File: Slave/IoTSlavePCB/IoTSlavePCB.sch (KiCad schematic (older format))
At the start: 0 parts

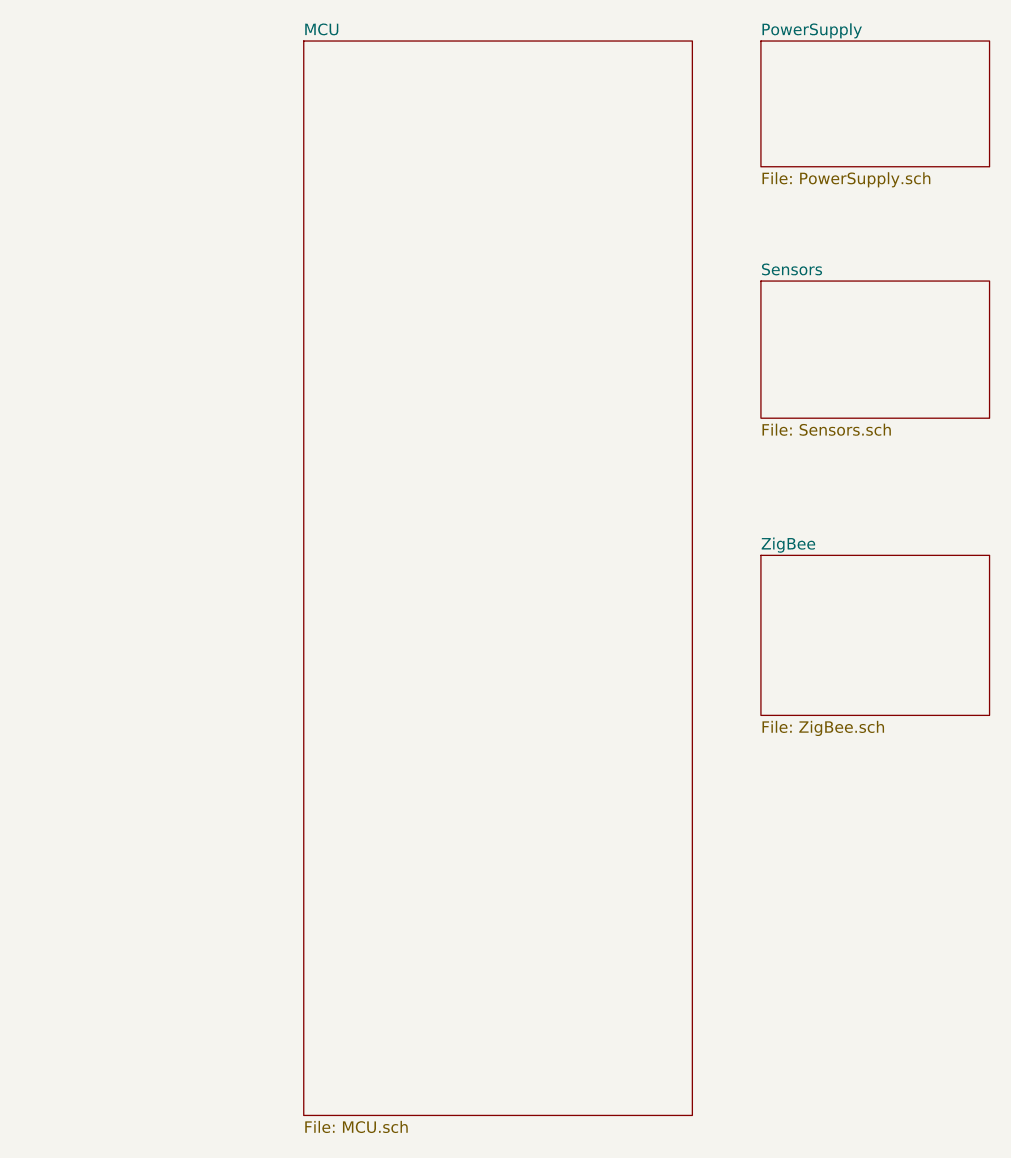
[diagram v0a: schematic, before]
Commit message: Continued work on slaves. Added sensor and begun work on ZigBee transceiver.
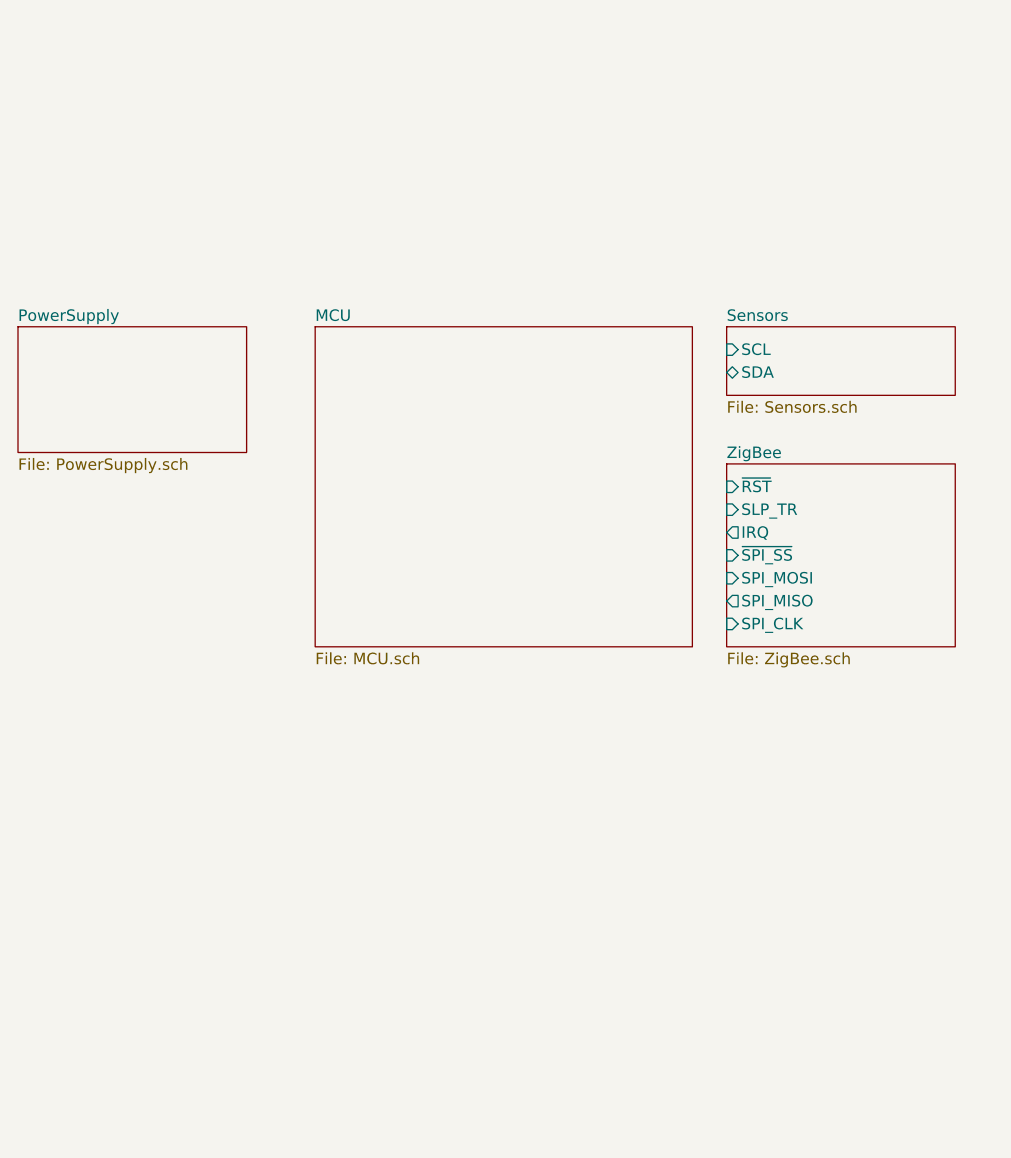
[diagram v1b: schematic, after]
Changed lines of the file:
@@
 $EndDescr
 $Sheet
-S 4700 1400 1700 4700
+S 4750 2650 1650 1400
 U 5F9E756E
 F0 "MCU" 50
@@
 $EndSheet
 $Sheet
-S 6700 1400 1000 550
+S 3450 2650 1000 550
 U 5F9F06B0
 F0 "PowerSupply" 50
@@
 $EndSheet
 $Sheet
-S 6700 2450 1000 600
+S 6550 2650 1000 300
 U 5F9F077B
 F0 "Sensors" 50
 F1 "Sensors.sch" 50
+F2 "SCL" I L 6550 2750 50
+F3 "SDA" B L 6550 2850 50
 $EndSheet
 $Sheet
-S 6700 3650 1000 700
+S 6550 3250 1000 800
 U 5F9F085D
 F0 "ZigBee" 50
 F1 "ZigBee.sch" 50
+F2 "~RST" I L 6550 3350 50
+F3 "SLP_TR" I L 6550 3450 50
+F4 "IRQ" O L 6550 3550 50
+F5 "~SPI_SS" I L 6550 3650 50
+F6 "SPI_MOSI" I L 6550 3750 50
+F7 "SPI_MISO" O L 6550 3850 50
+F8 "SPI_CLK" I L 6550 3950 50
 $EndSheet
 $EndSCHEMATC

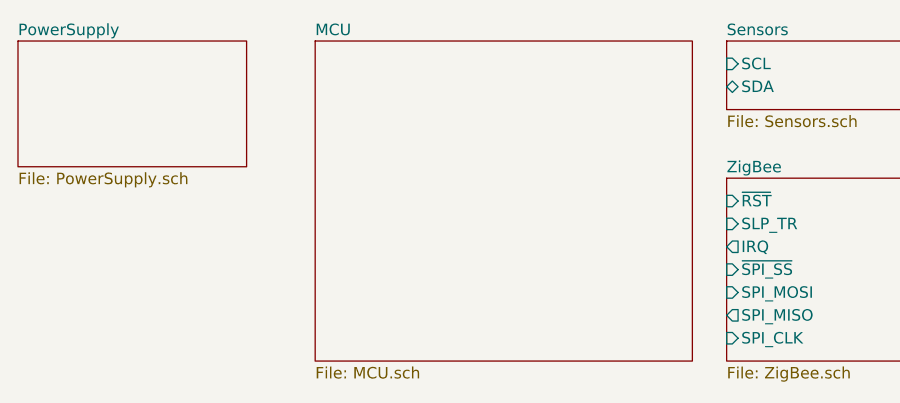
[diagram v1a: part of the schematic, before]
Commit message: Finished slave schematics, including memory and Zigbee Transceiver. Further work on PCB, well underway.
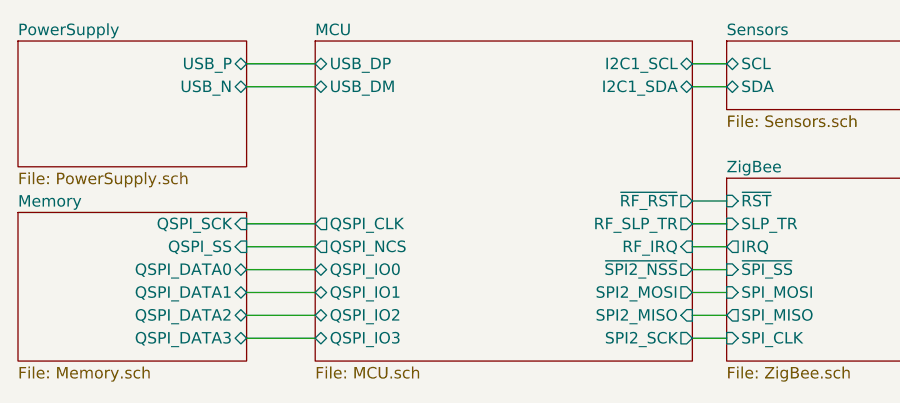
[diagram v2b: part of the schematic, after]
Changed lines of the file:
@@
 $Descr A4 11693 8268
 encoding utf-8
-Sheet 1 5
+Sheet 1 6
 Title "IoT Slave Board"
 Date "2020-11-01"
@@
 F0 "MCU" 50
 F1 "MCU.sch" 50
+F2 "I2C1_SCL" B R 6400 2750 50
+F3 "I2C1_SDA" B R 6400 2850 50
+F4 "~SPI2_NSS" O R 6400 3650 50
+F5 "SPI2_MOSI" O R 6400 3750 50
+F6 "SPI2_SCK" O R 6400 3950 50
+F7 "SPI2_MISO" I R 6400 3850 50
+F8 "RF_IRQ" I R 6400 3550 50
+F9 "RF_SLP_TR" O R 6400 3450 50
+F10 "~RF_RST" O R 6400 3350 50
+F11 "USB_DP" B L 4750 2750 50
+F12 "USB_DM" B L 4750 2850 50
+F13 "QSPI_CLK" O L 4750 3450 50
+F14 "QSPI_NCS" O L 4750 3550 50
+F15 "QSPI_IO0" B L 4750 3650 50
+F16 "QSPI_IO1" B L 4750 3750 50
+F17 "QSPI_IO2" B L 4750 3850 50
+F18 "QSPI_IO3" B L 4750 3950 50
 $EndSheet
 $Sheet
@@
 F0 "PowerSupply" 50
 F1 "PowerSupply.sch" 50
+F2 "USB_P" B R 4450 2750 50
+F3 "USB_N" B R 4450 2850 50
 $EndSheet
 $Sheet
@@
 F0 "Sensors" 50
 F1 "Sensors.sch" 50
-F2 "SCL" I L 6550 2750 50
+F2 "SCL" B L 6550 2750 50
 F3 "SDA" B L 6550 2850 50
 $EndSheet
@@
 F8 "SPI_CLK" I L 6550 3950 50
 $EndSheet
+Wire Wire Line
+	6400 2750 6550 2750
+Wire Wire Line
+	6550 2850 6400 2850
+Wire Wire Line
+	6400 3350 6550 3350
+Wire Wire Line
+	6550 3450 6400 3450
+Wire Wire Line
+	6400 3550 6550 3550
+Wire Wire Line
+	6550 3650 6400 3650
+Wire Wire Line
+	6400 3750 6550 3750
+Wire Wire Line
+	6550 3850 6400 3850
+Wire Wire Line
+	6400 3950 6550 3950
+$Sheet
+S 3450 3400 1000 650
+U 5FB49FC4
+F0 "Memory" 50
+F1 "Memory.sch" 50
+F2 "QSPI_SCK" I R 4450 3450 50
+F3 "QSPI_SS" I R 4450 3550 50
+F4 "QSPI_DATA0" B R 4450 3650 50
+F5 "QSPI_DATA1" B R 4450 3750 50
+F6 "QSPI_DATA2" B R 4450 3850 50
+F7 "QSPI_DATA3" B R 4450 3950 50
+$EndSheet
+Wire Wire Line
+	4450 3450 4750 3450
+Wire Wire Line
+	4750 3550 4450 3550
+Wire Wire Line
+	4450 3650 4750 3650
+Wire Wire Line
+	4750 3750 4450 3750
+Wire Wire Line
+	4450 3850 4750 3850
+Wire Wire Line
+	4750 3950 4450 3950
+Wire Wire Line
+	4450 2750 4750 2750
+Wire Wire Line
+	4750 2850 4450 2850
 $EndSCHEMATC

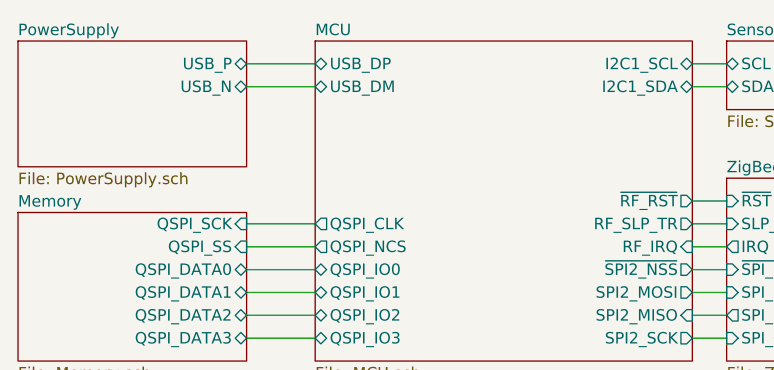
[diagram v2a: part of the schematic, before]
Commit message: Made more connections on PCB, some optimizations. Added silk screen text.
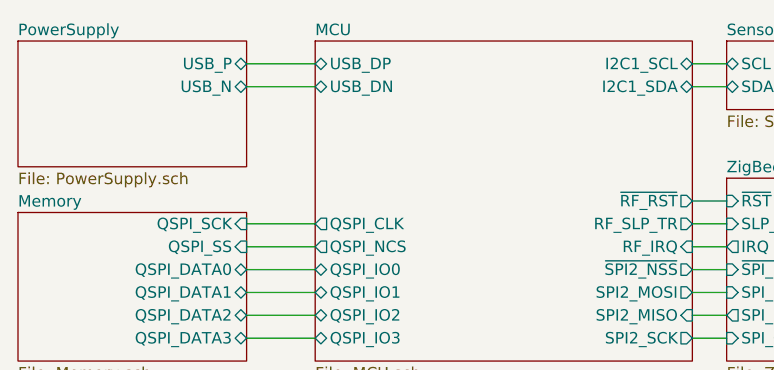
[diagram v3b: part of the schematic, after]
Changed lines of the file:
@@
 F10 "~RF_RST" O R 6400 3350 50
 F11 "USB_DP" B L 4750 2750 50
-F12 "USB_DM" B L 4750 2850 50
+F12 "USB_DN" B L 4750 2850 50
 F13 "QSPI_CLK" O L 4750 3450 50
 F14 "QSPI_NCS" O L 4750 3550 50

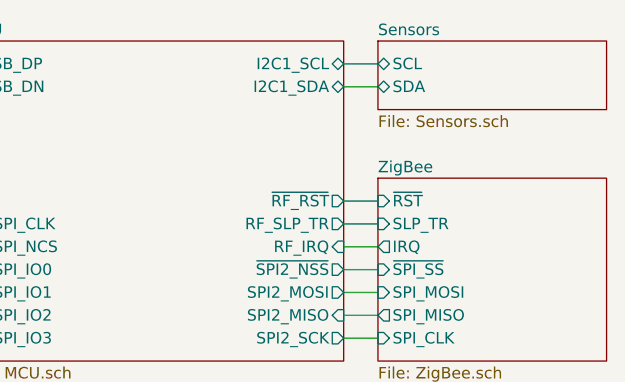
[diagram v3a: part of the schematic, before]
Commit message: Added battery voltage measurement circuit. Optimizations to antenna and general component placement.
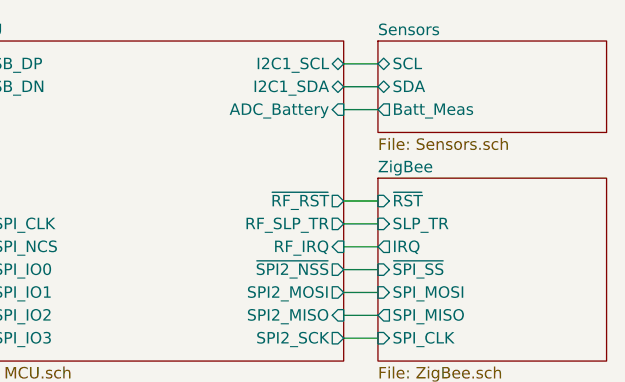
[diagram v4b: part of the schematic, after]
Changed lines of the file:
@@
 F17 "QSPI_IO2" B L 4750 3850 50
 F18 "QSPI_IO3" B L 4750 3950 50
+F19 "ADC_Battery" I R 6400 2950 50
 $EndSheet
 $Sheet
@@
 $EndSheet
 $Sheet
-S 6550 2650 1000 300
+S 6550 2650 1000 400
 U 5F9F077B
 F0 "Sensors" 50
@@
 F2 "SCL" B L 6550 2750 50
 F3 "SDA" B L 6550 2850 50
+F4 "Batt_Meas" O L 6550 2950 50
 $EndSheet
 $Sheet
@@
 Wire Wire Line
 	4750 2850 4450 2850
+Wire Wire Line
+	6550 2950 6400 2950
 $EndSCHEMATC
